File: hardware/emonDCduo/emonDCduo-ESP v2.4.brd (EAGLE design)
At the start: 114.2 x 76.5 mm, 112 parts, among them IC1 ACS758LCB-050B-PFF-T, IC2 ACS758LCB-050B-PFF-T, IC3 ACS758LCB-050B-PFF-T, IC4 ACS758LCB-050B-PFF-T, P1 B4B-PH-K, X3 GMSTBV2, X4 GMSTBV2, Y1 32Khz

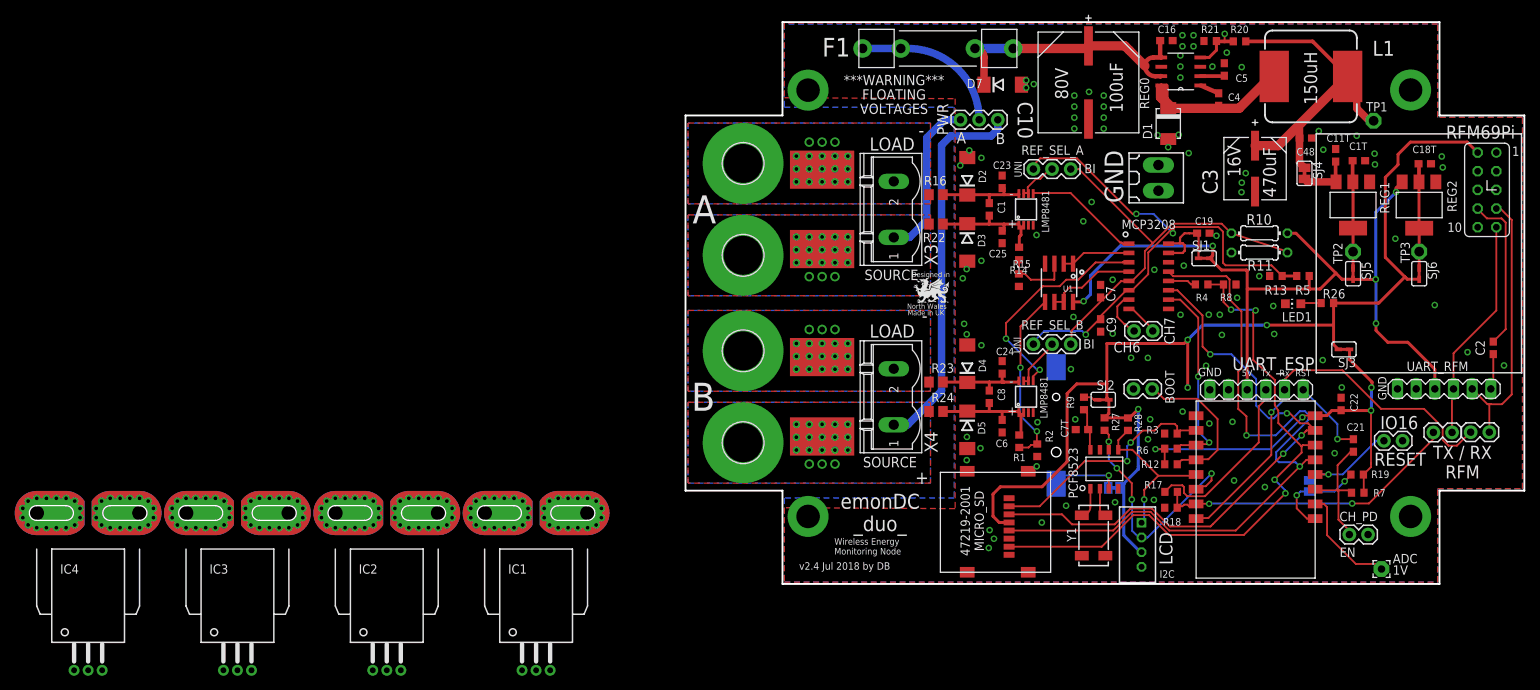
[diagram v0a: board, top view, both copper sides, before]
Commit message: starting v3.0 and ASC770 breakout
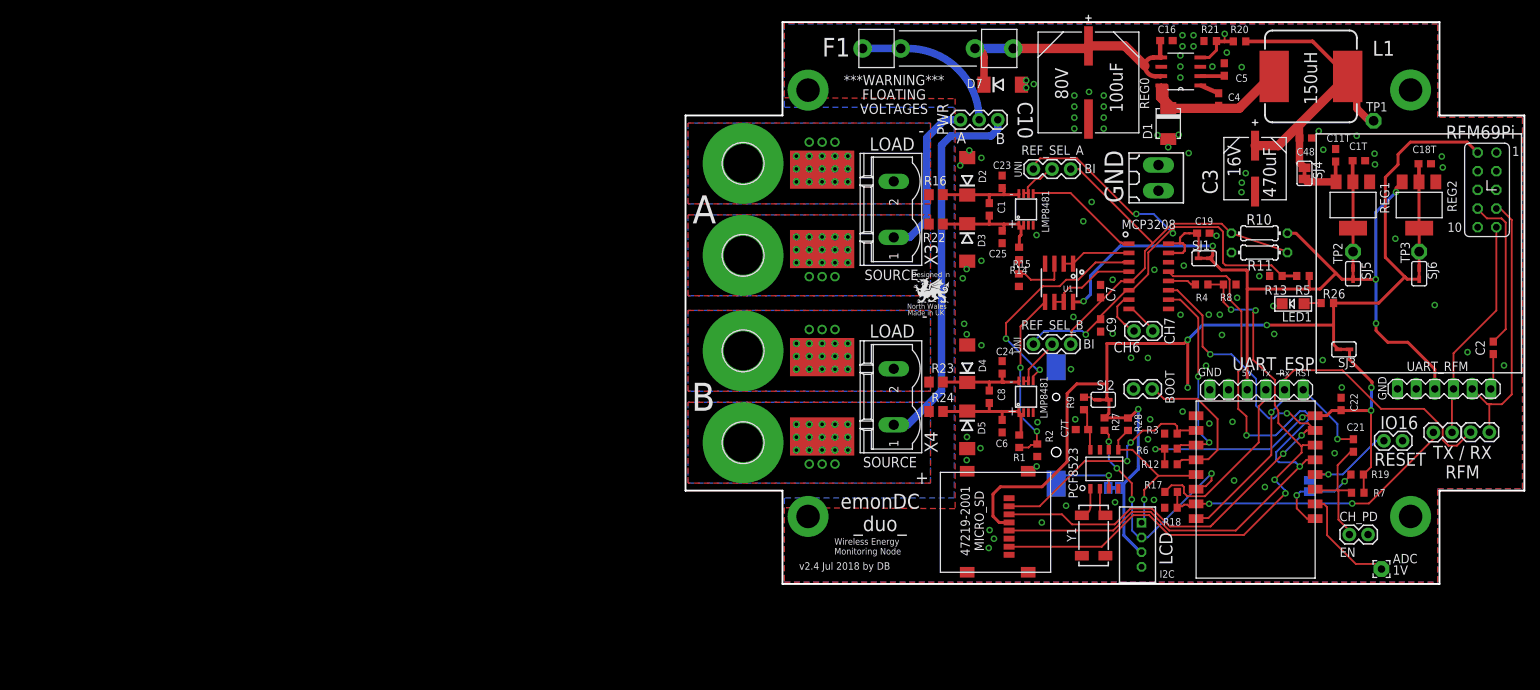
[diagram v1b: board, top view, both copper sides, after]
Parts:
- removed IC1, IC2, IC3, IC4: ACS758LCB-050B-PFF-T, allegro:CB-PFF
- LED1: device led:CHIP-LED0805 -> microbuilder:CHIPLED_1206
- R10: value 16.56k -> 32k
- R11, R13: value 5.23k -> 10k
- R26: value 1K -> 390R
- R5: value 517.77k -> 1M
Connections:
- removed net VCC: IC1.1, IC2.1, IC3.1, IC4.1
- net GND: no longer IC1.2, IC2.2, IC3.2, IC4.2
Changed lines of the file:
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@@
 <attribute name="VALUE" x="33.095" y="27.885" size="1.27" layer="27" rot="R270"/>
 </element>
-<element name="R10" library="rcl" library_urn="urn:adsk.eagle:library:334" package="0204/7" package3d_urn="urn:adsk.eagle:package:23498/1" value="16.56k" x="71.758" y="49.504" smashed="yes">
+<element name="R10" library="rcl" library_urn="urn:adsk.eagle:library:334" package="0204/7" package3d_urn="urn:adsk.eagle:package:23498/1" value="32k" x="71.758" y="49.504" smashed="yes">
 <attribute name="NAME" x="69.988" y="50.6724" size="1.4224" layer="25" ratio="10"/>
 <attribute name="SPICEPREFIX" value="R" x="71.758" y="49.504" size="1.778" layer="27" display="off"/>
 <attribute name="VALUE" x="70.1324" y="49.0214" size="0.9906" layer="27" ratio="10"/>
 </element>
-<element name="R11" library="rcl" library_urn="urn:adsk.eagle:library:334" package="0204/7" package3d_urn="urn:adsk.eagle:package:23498/1" value="5.23k" x="71.758" y="46.877" smashed="yes">
+<element name="R11" library="rcl" library_urn="urn:adsk.eagle:library:334" package="0204/7" package3d_urn="urn:adsk.eagle:package:23498/1" value="10k" x="71.758" y="46.877" smashed="yes">
 <attribute name="NAME" x="70.115" y="44.4184" size="1.4224" layer="25" ratio="10"/>
 <attribute name="SPICEPREFIX" value="R" x="71.758" y="46.877" size="1.778" layer="27" display="off"/>
@@
 <attribute name="VALUE" x="63.492065625" y="47.61025" size="1.27" layer="27"/>
 </element>
-<element name="R26" library="rcl" library_urn="urn:adsk.eagle:library:334" package="R0603" package3d_urn="urn:adsk.eagle:package:23555/2" value="1K" x="81" y="40" smashed="yes">
+<element name="R26" library="rcl" library_urn="urn:adsk.eagle:library:334" package="R0603" package3d_urn="urn:adsk.eagle:package:23555/2" value="390R" x="81" y="40" smashed="yes">
 <attribute name="NAME" x="80.365" y="40.635" size="1.27" layer="25"/>
 <attribute name="SPICEPREFIX" value="R" x="81" y="40" size="1.778" layer="27" display="off"/>
 <attribute name="VALUE" x="80.365" y="38.095" size="1.27" layer="27"/>
 </element>
-<element name="LED1" library="led" library_urn="urn:adsk.eagle:library:259" package="CHIP-LED0805" package3d_urn="urn:adsk.eagle:package:15818/2" value="" x="76.348" y="39.908" smashed="yes" rot="R90">
+<element name="LED1" library="microbuilder" package="CHIPLED_1206" value="" x="76.348" y="39.908" smashed="yes" rot="R90">
 <attribute name="NAME" x="78.888" y="38.765" size="1.27" layer="25" rot="R180"/>
 <attribute name="VALUE" x="77.618" y="42.448" size="1.27" layer="27" rot="R180"/>
@@
 <attribute name="VALUE" x="52.047603125" y="40.98534375" size="1.27" layer="27" rot="R90"/>
 </element>
-<element name="R5" library="rcl7" package="R0603" value="517.77k" x="77.685" y="43.688" smashed="yes" rot="R180">
+<element name="R5" library="rcl7" package="R0603" value="1M" x="77.685" y="43.688" smashed="yes" rot="R180">
 <attribute name="NAME" x="78.701" y="42.418" size="1.27" layer="25" rot="R180"/>
 <attribute name="VALUE" x="78.32" y="45.593" size="1.27" layer="27" rot="R180"/>
 </element>
-<element name="R13" library="rcl7" package="R0603" value="5.23k" x="74.002" y="43.688" smashed="yes" rot="R180">
+<element name="R13" library="rcl7" package="R0603" value="10k" x="74.002" y="43.688" smashed="yes" rot="R180">
 <attribute name="NAME" x="75.526" y="42.418" size="1.27" layer="25" rot="R180"/>
 <attribute name="VALUE" x="74.637" y="45.593" size="1.27" layer="27" rot="R180"/>
@@
 <attribute name="NAME" x="81.153" y="16.002" size="1.27" layer="26" ratio="10" rot="MR270"/>
 <attribute name="VALUE" x="78.613" y="14.7129" size="0.02" layer="28" rot="MR270"/>
-</element>
-<element name="IC1" library="allegro" library_urn="urn:adsk.eagle:library:93" package="CB-PFF" package3d_urn="urn:adsk.eagle:package:3449/1" value="ACS758LCB-050B-PFF-T" x="-26.67" y="11.43" smashed="yes">
-<attribute name="MF" value="" x="-26.67" y="11.43" size="1.778" layer="27" display="off"/>
-<attribute name="MPN" value="ACS758LCB-050B-PFF-T" x="-26.67" y="11.43" size="1.778" layer="27" display="off"/>
-<attribute name="NAME" x="-30.48" y="3.175" size="1.27" layer="25"/>
-<attribute name="OC_FARNELL" value="1718997" x="-26.67" y="11.43" size="1.778" layer="27" display="off"/>
-<attribute name="OC_NEWARK" value="04R7131" x="-26.67" y="11.43" size="1.778" layer="27" display="off"/>
-<attribute name="VALUE" x="-30.48" y="-1.905" size="1.27" layer="27"/>
-</element>
-<element name="IC2" library="allegro" library_urn="urn:adsk.eagle:library:93" package="CB-PFF" package3d_urn="urn:adsk.eagle:package:3449/1" value="ACS758LCB-050B-PFF-T" x="-46.99" y="11.43" smashed="yes">
-<attribute name="MF" value="" x="-46.99" y="11.43" size="1.778" layer="27" display="off"/>
-<attribute name="MPN" value="ACS758LCB-050B-PFF-T" x="-46.99" y="11.43" size="1.778" layer="27" display="off"/>
-<attribute name="NAME" x="-50.8" y="3.175" size="1.27" layer="25"/>
-<attribute name="OC_FARNELL" value="1718997" x="-46.99" y="11.43" size="1.778" layer="27" display="off"/>
-<attribute name="OC_NEWARK" value="04R7131" x="-46.99" y="11.43" size="1.778" layer="27" display="off"/>
-<attribute name="VALUE" x="-50.8" y="-1.905" size="1.27" layer="27"/>
-</element>
-<element name="IC3" library="allegro" library_urn="urn:adsk.eagle:library:93" package="CB-PFF" package3d_urn="urn:adsk.eagle:package:3449/1" value="ACS758LCB-050B-PFF-T" x="-67.31" y="11.43" smashed="yes">
-<attribute name="MF" value="" x="-67.31" y="11.43" size="1.778" layer="27" display="off"/>
-<attribute name="MPN" value="ACS758LCB-050B-PFF-T" x="-67.31" y="11.43" size="1.778" layer="27" display="off"/>
-<attribute name="NAME" x="-71.12" y="3.175" size="1.27" layer="25"/>
-<attribute name="OC_FARNELL" value="1718997" x="-67.31" y="11.43" size="1.778" layer="27" display="off"/>
-<attribute name="OC_NEWARK" value="04R7131" x="-67.31" y="11.43" size="1.778" layer="27" display="off"/>
-<attribute name="VALUE" x="-71.12" y="-1.905" size="1.27" layer="27"/>
-</element>
-<element name="IC4" library="allegro" library_urn="urn:adsk.eagle:library:93" package="CB-PFF" package3d_urn="urn:adsk.eagle:package:3449/1" value="ACS758LCB-050B-PFF-T" x="-87.63" y="11.43" smashed="yes">
-<attribute name="MF" value="" x="-87.63" y="11.43" size="1.778" layer="27" display="off"/>
-<attribute name="MPN" value="ACS758LCB-050B-PFF-T" x="-87.63" y="11.43" size="1.778" layer="27" display="off"/>
-<attribute name="NAME" x="-91.44" y="3.175" size="1.27" layer="25"/>
-<attribute name="OC_FARNELL" value="1718997" x="-87.63" y="11.43" size="1.778" layer="27" display="off"/>
-<attribute name="OC_NEWARK" value="04R7131" x="-87.63" y="11.43" size="1.778" layer="27" display="off"/>
-<attribute name="VALUE" x="-91.44" y="-1.905" size="1.27" layer="27"/>
 </element>
 </elements>
@@
 <via x="100.081071875" y="33.323209375" extent="1-16" drill="0.5"/>
 <via x="105.04284375" y="31.5111875" extent="1-16" drill="0.5"/>
-<contactref element="IC1" pad="2"/>
-<contactref element="IC2" pad="2"/>
-<contactref element="IC3" pad="2"/>
-<contactref element="IC4" pad="2"/>
 <wire x1="84.99694375" y1="62.77434375" x2="92.332925" y2="68.99475" width="0" layer="19" extent="1-1"/>
 <wire x1="82.133790625" y1="60.964315625" x2="84.99694375" y2="62.77434375" width="0" layer="19" extent="1-1"/>
@@
 <wire x1="59.391" y1="39.201" x2="61.0232625" y2="38.41541875" width="0" layer="19" extent="1-1"/>
 <wire x1="73.64371875" y1="39.60443125" x2="73.152" y2="43.688" width="0" layer="19" extent="1-1"/>
-<wire x1="75.298" y1="39.908" x2="73.64371875" y2="39.60443125" width="0" layer="19" extent="1-1"/>
+<wire x1="74.852" y1="39.908" x2="73.64371875" y2="39.60443125" width="0" layer="19" extent="1-1"/>
 <wire x1="73.77071875" y1="35.79443125" x2="73.64371875" y2="39.60443125" width="0" layer="19" extent="1-1"/>
 <wire x1="64.49971875" y1="31.47643125" x2="66.65871875" y2="35.66743125" width="0" layer="19" extent="1-1"/>
@@
 <wire x1="10.338628125" y1="10.96651875" x2="31.993665625" y2="17.11694375" width="0" layer="19" extent="1-1"/>
 <wire x1="10.338628125" y1="68.97651875" x2="31.049528125" y2="58.720834375" width="0" layer="19" extent="1-1"/>
-<wire x1="-26.67" y1="-9.97" x2="10.338628125" y2="10.96651875" width="0" layer="19" extent="1-1"/>
-<wire x1="-46.99" y1="-9.97" x2="-26.67" y2="-9.97" width="0" layer="19" extent="1-1"/>
-<wire x1="-67.31" y1="-9.97" x2="-46.99" y2="-9.97" width="0" layer="19" extent="1-1"/>
-<wire x1="-87.63" y1="-9.97" x2="-67.31" y2="-9.97" width="0" layer="19" extent="1-1"/>
 </signal>
 <signal name="+3V3" class="2">
@@
 <wire x1="77.6097" y1="40.005" x2="80.1243" y2="40.005" width="0.254" layer="1"/>
 <wire x1="80.1243" y1="40.005" x2="80.15" y2="40" width="0.254" layer="1"/>
-<wire x1="77.6097" y1="40.005" x2="77.398" y2="39.908" width="0.254" layer="1"/>
+<wire x1="77.6097" y1="40.005" x2="77.844" y2="39.908" width="0.254" layer="1"/>
 </signal>
 <signal name="MCP_VCC">
@@
 <wire x1="84.213721875" y1="16.602921875" x2="84.213721875" y2="16.66411875" width="0.254" layer="1"/>
 </signal>
-<signal name="VCC">
-<contactref element="IC1" pad="1"/>
-<contactref element="IC2" pad="1"/>
-<contactref element="IC3" pad="1"/>
-<contactref element="IC4" pad="1"/>
-<wire x1="-69.22" y1="-9.97" x2="-89.54" y2="-9.97" width="0" layer="19" extent="1-1"/>
-<wire x1="-48.9" y1="-9.97" x2="-69.22" y2="-9.97" width="0" layer="19" extent="1-1"/>
-<wire x1="-28.58" y1="-9.97" x2="-48.9" y2="-9.97" width="0" layer="19" extent="1-1"/>
-</signal>
 </signals>

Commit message: commit v3.0
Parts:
- C11T, C18T, C1T: device rcl:C0603 -> rcl7:C0603POL
- C7T: device rcl@1:C0603 -> rcl7:C0603POL
- R10, R11: device rcl:0204/7 -> rcl7:0207/10
- R16, R22, R23, R24: device rcl:R0805 -> rcl7:R1206
- moved LED1 2.50 mm to (77.6, 37.7)
- moved R26 2.29 mm to (82.9, 38.7)
- moved C3 2.07 mm to (69.3, 59.2)
- moved D2 1.91 mm to (33.9, 57.2)
- moved D3 1.91 mm to (33.9, 48.2)
- moved D4 1.91 mm to (33.9, 31.8)
- moved D5 1.91 mm to (33.9, 22.8)
- moved R16 1.91 mm to (29.7, 54.8)
- moved R22 1.91 mm to (29.7, 50.8)
- moved R23 1.91 mm to (29.7, 29.2)
- moved R24 1.91 mm to (29.7, 25.2)
- moved R13 1.52 mm to (74.0, 42.2)
- moved R5 1.40 mm to (77.7, 42.3)
- moved R11 1.30 mm to (73.0, 46.6)
- moved R10 1.27 mm to (73.0, 49.5)
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- renumbered U1 to LM258
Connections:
- removed net CH6: J5.2, MCP3208.7
- net +3V3: now also MCP3208.7
- net GND: now also J5.2
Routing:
- net +5V: track 111.5 -> 88.9 mm
- net +3V3: track 159.3 -> 168.7 mm, vias 4 -> 5
- net LOAD-NEG-A: track 0.00 -> 6.60 mm
- net LOAD-NEG-B: track 0.00 -> 6.53 mm
- net CH6: track 6.47 -> 0.00 mm
- net SOURCE-POS-A: track 22.3 -> 28.5 mm
- net SOURCE-POS-B: track 51.7 -> 57.9 mm
- net REF_A_INPUT: track 5.91 -> 8.98 mm
- net SOURCE-POS-B_T: track 17.0 -> 14.4 mm
- net SOURCE-POS-A_T: track 16.6 -> 14.2 mm
- net LOAD-NEG-A_T: track 12.8 -> 10.5 mm
- net CH7: track 4.65 -> 6.37 mm, vias 0 -> 1
- net PRE_6.5V: track 46.7 -> 48.2 mm
- net SCL: track 35.9 -> 34.5 mm
- net BI_REF: track 55.7 -> 56.9 mm, vias 0 -> 1
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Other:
- board text added: "REF"
- board text removed: "BI"
- board text removed: "CH6"
